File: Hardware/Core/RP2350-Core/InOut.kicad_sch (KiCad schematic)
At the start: 15 parts, among them CN10 PR5L4015-5P-C-F, CN11 PR5L4015-5P-C-F, CN7 PR5L4015-5P-C-F, CN8 PR5L4015-5P-C-F, CN9 PR5L4015-5P-C-F, J3 Conn_01x10_Socket, J4 Conn_01x10_Socket, U35 PR5L5015-5P-C-H, U36 PR5L5015-5P-C-H, U37 PR5L5015-5P-C-H, U38 PR5L5015-5P-C-H, U39 PR5L5015-5P-C-H

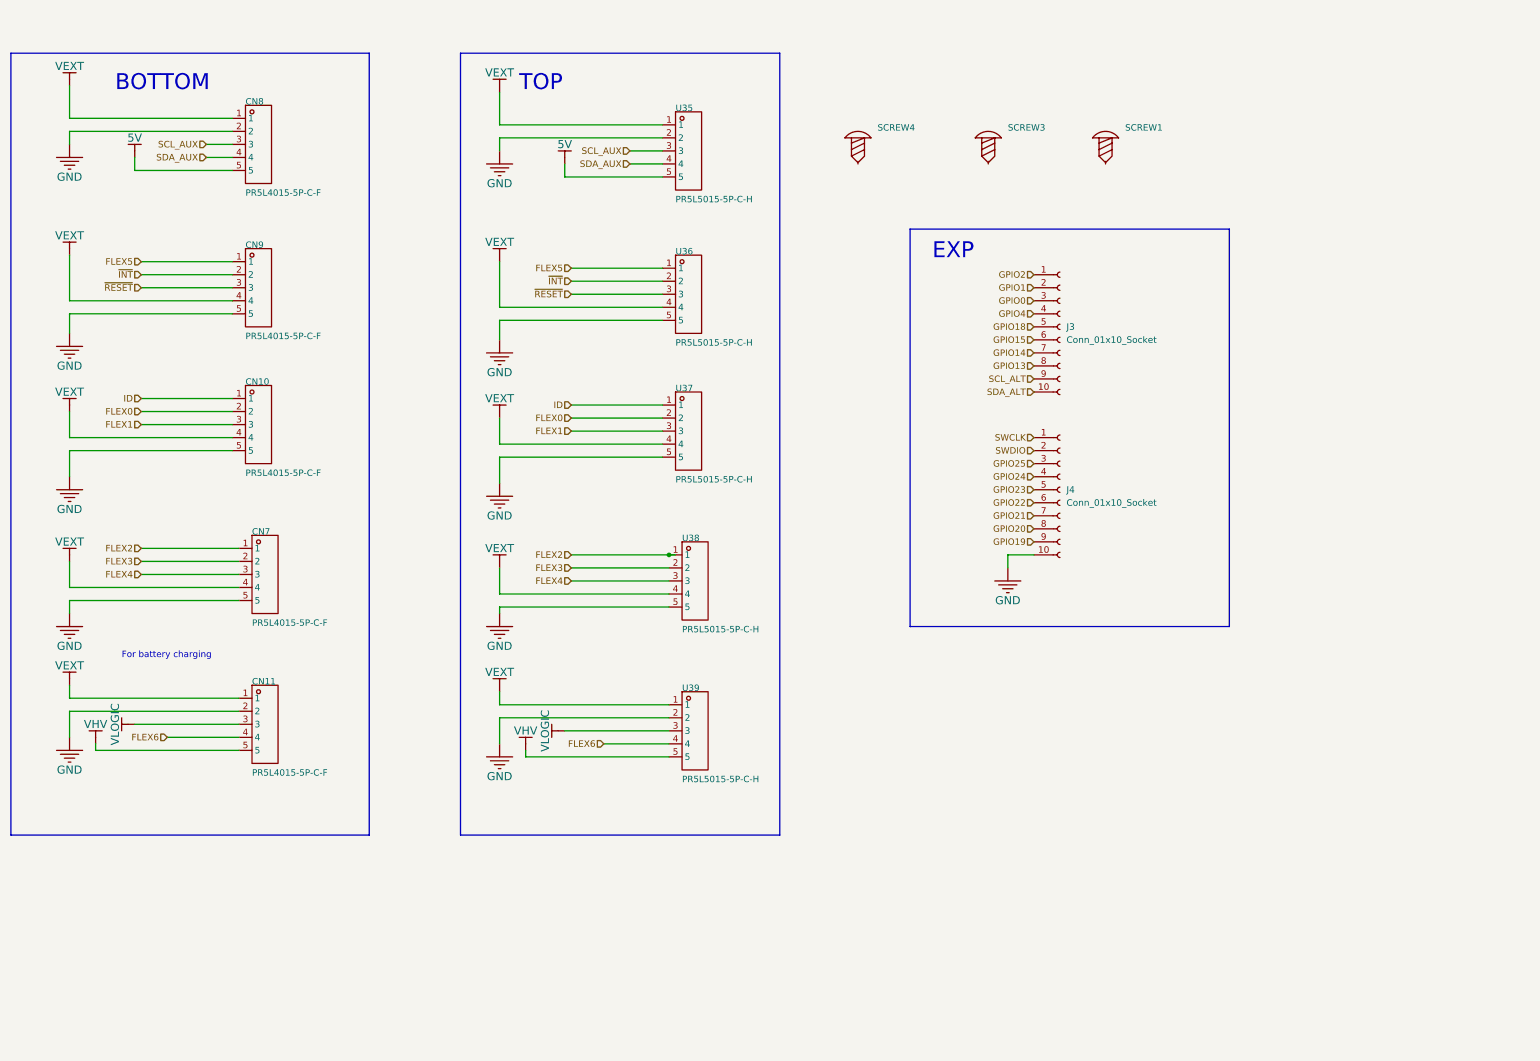
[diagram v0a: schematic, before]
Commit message: Added RP2354 with integrated flash, 80 pin and OR diode in power supply
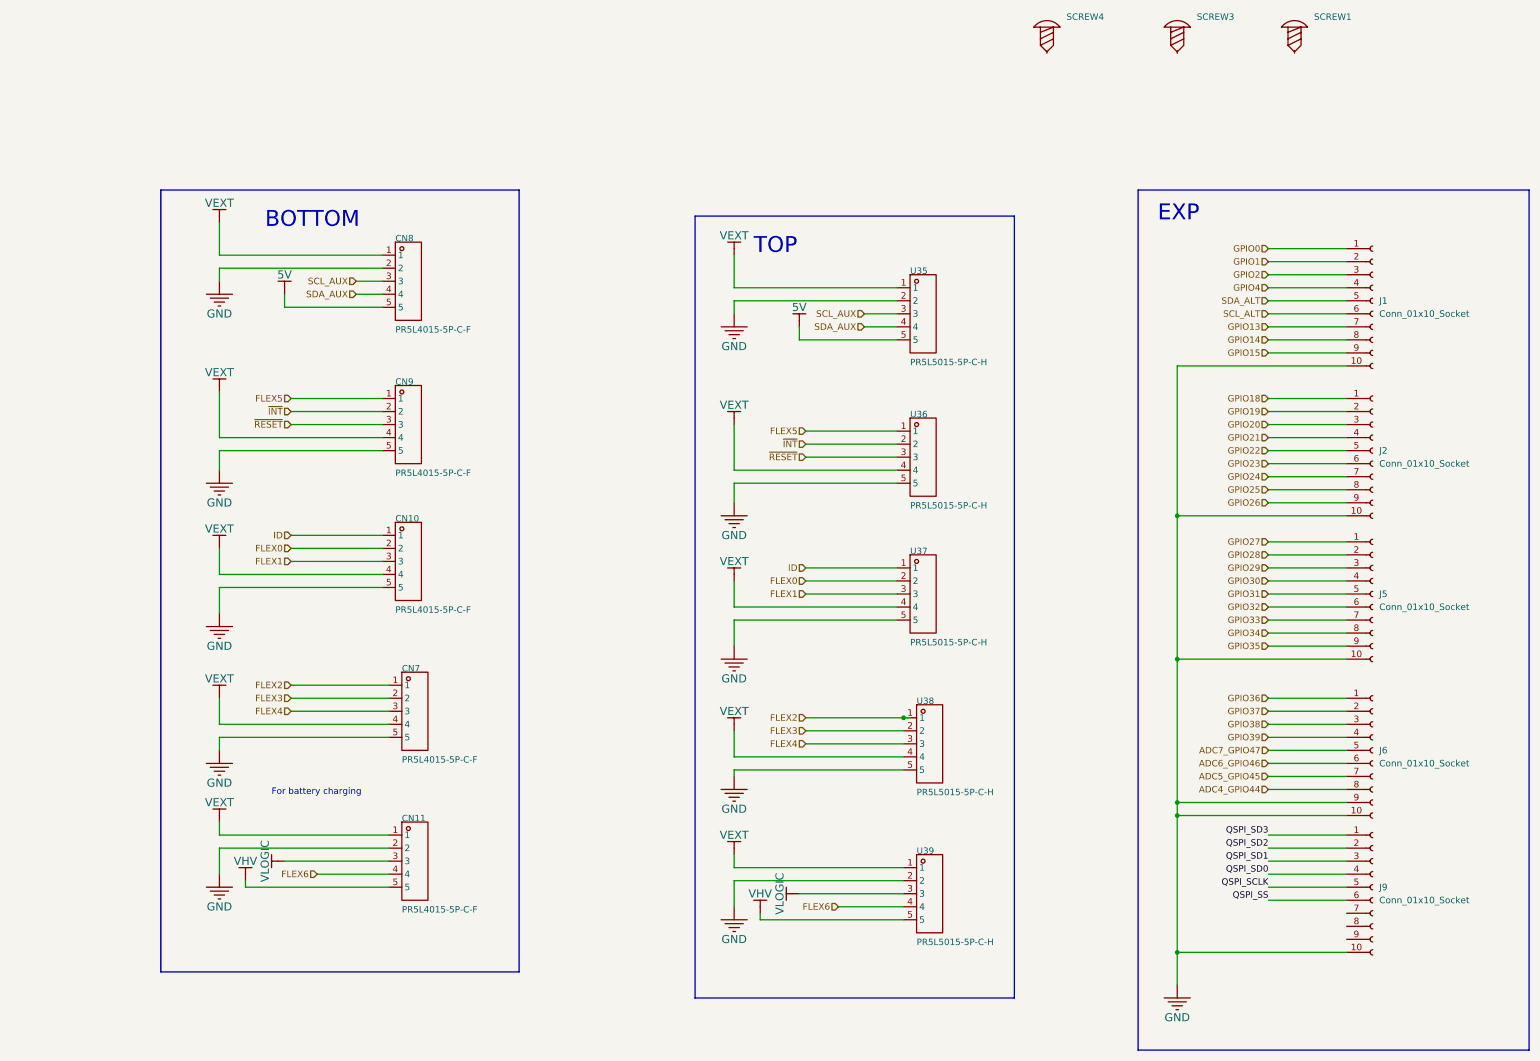
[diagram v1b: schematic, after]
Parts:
- removed J3, J4: Conn_01x10_Socket, symbol Connector:Conn_01x10_Socket
- added J1, J2, J5, J6, J9: Conn_01x10_Socket, symbol Connector:Conn_01x10_Socket
- CN10, CN11, CN7, CN8, CN9: footprint USBC_PD_mo-easyedapro:CONN-TH_PR5L4015-5P-C-F -> SpaghettiLAB:CONN-TH_PR5L4015-5P-C-F
- U35, U36, U37, U38, U39: footprint USBC_PD_mo-easyedapro:CONN-TH_PR5L5015-5P-C-H -> SpaghettiLAB:CONN-TH_PR5L5015-5P-C-H
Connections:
- net GND: now also J1.10 (Pin_10), J2.10 (Pin_10), J5.10 (Pin_10), J6.10 (Pin_10), J6.9 (Pin_9), J9.10 (Pin_10)
- net GPIO0: now also J1.1 (Pin_1)
- net GPIO1: now also J1.2 (Pin_2)
- net GPIO13: now also J1.7 (Pin_7)
- net GPIO14: now also J1.8 (Pin_8)
- net GPIO15: now also J1.9 (Pin_9)
- net GPIO18: now also J2.1 (Pin_1)
- net GPIO19: now also J2.2 (Pin_2)
- net GPIO2: now also J1.3 (Pin_3)
- net GPIO20: now also J2.3 (Pin_3)
- net GPIO21: now also J2.4 (Pin_4)
- net GPIO22: now also J2.5 (Pin_5)
- net GPIO23: now also J2.6 (Pin_6)
- net GPIO24: now also J2.7 (Pin_7)
- net GPIO25: now also J2.8 (Pin_8)
- net GPIO4: now also J1.4 (Pin_4)
- net SCL_ALT: now also J1.6 (Pin_6)
- net SDA_ALT: now also J1.5 (Pin_5)
- new net GPIO26: J2.9 (Pin_9)
- new net GPIO27: J5.1 (Pin_1)
- new net GPIO28: J5.2 (Pin_2)
- new net GPIO29: J5.3 (Pin_3)
- new net GPIO30: J5.4 (Pin_4)
- new net GPIO31: J5.5 (Pin_5)
- new net GPIO32: J5.6 (Pin_6)
- new net GPIO33: J5.7 (Pin_7)
- new net GPIO34: J5.8 (Pin_8)
- new net GPIO35: J5.9 (Pin_9)
- new net GPIO36: J6.1 (Pin_1)
- new net GPIO37: J6.2 (Pin_2)
- new net GPIO38: J6.3 (Pin_3)
- new net GPIO39: J6.4 (Pin_4)
- new net QSPI_SCLK: J9.5 (Pin_5)
- new net QSPI_SD0: J9.4 (Pin_4)
- new net QSPI_SD1: J9.3 (Pin_3)
- new net QSPI_SD2: J9.2 (Pin_2)
- new net QSPI_SD3: J9.1 (Pin_1)
- new net QSPI_SS: J9.6 (Pin_6)
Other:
- moved on the sheet: CN10, CN11, CN7, CN8, CN9, SCREW1, SCREW3, SCREW4, U35, U36, U37, U38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

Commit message: Use shared SpaghettiLAB libraries with portable relative paths
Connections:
- net GPIO39 is gone; now on net ADC7_GPIO47: J6.4 (Pin_4)
- net ADC4_GPIO44: now also J6.7 (Pin_7)
- net ADC5_GPIO45: now also J6.6 (Pin_6)
- net ADC6_GPIO46: now also J6.5 (Pin_5)
- net GND: now also J6.8 (Pin_8), J9.7 (Pin_7), J9.8 (Pin_8), J9.9 (Pin_9)

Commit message: schematic done, missing pogo expansion pin component selection
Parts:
- SCREW1, SCREW3, SCREW4: footprint USBC_PD_mo-easyedapro:Screw-Hole-M2 -> MountingHole:MountingHole_2.2mm_M2
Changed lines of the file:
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@@
 			)
 		)
-		(property "Footprint" "USBC_PD_mo-easyedapro:Screw-Hole-M2"
+		(property "Footprint" "MountingHole:MountingHole_2.2mm_M2"
 			(at 222.25 30.48 0)
 			(hide yes)
@@
 			)
 		)
-		(property "Footprint" "USBC_PD_mo-easyedapro:Screw-Hole-M2"
+		(property "Footprint" "MountingHole:MountingHole_2.2mm_M2"
 			(at 247.65 30.48 0)
 			(hide yes)
@@
 			)
 		)
-		(property "Footprint" "USBC_PD_mo-easyedapro:Screw-Hole-M2"
+		(property "Footprint" "MountingHole:MountingHole_2.2mm_M2"
 			(at 270.51 30.48 0)
 			(hide yes)

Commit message: Footprint assigned core rp2350
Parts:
- removed SCREW1, SCREW3, SCREW4: (no value), MountingHole:MountingHole_2.2mm_M2, symbol USBC_PD_mo-easyedapro:Screw-Hole
- added H1, H2, H3, H4: MountingHole, MountingHole:MountingHole_2.2mm_M2, symbol Mechanical:MountingHole
- J1, J2, J5, J6, J9: footprint (none) -> Connector_PinHeader_2.54mm:PinHeader_2x10_P2.54mm_Vertical
